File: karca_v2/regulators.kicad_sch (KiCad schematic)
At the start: 23 parts, among them J1 CON_FAN1, J2 Conn_Batt, SW1 SW_SPST, SW2 SW_SPST, SW3 SW_SPST, U1 TVS1400DRV

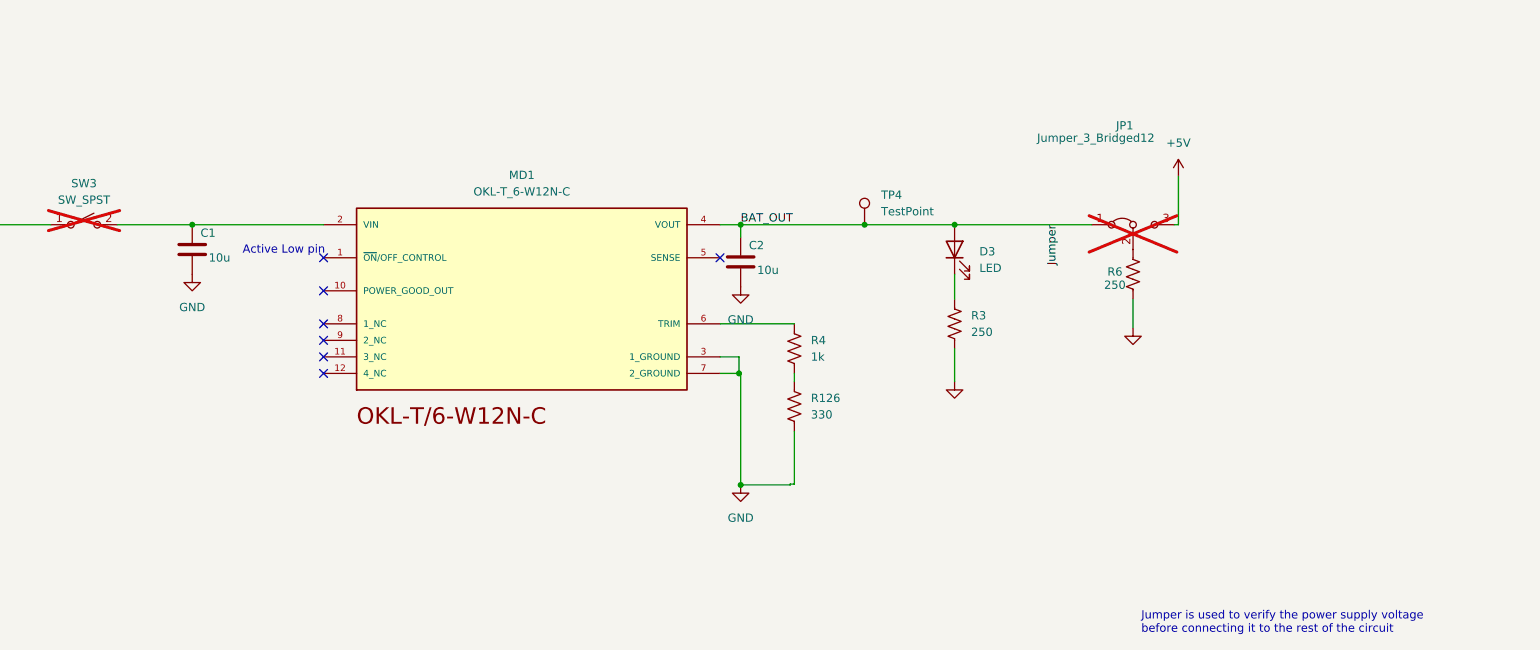
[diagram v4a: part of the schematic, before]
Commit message: finished schematic for v2.1
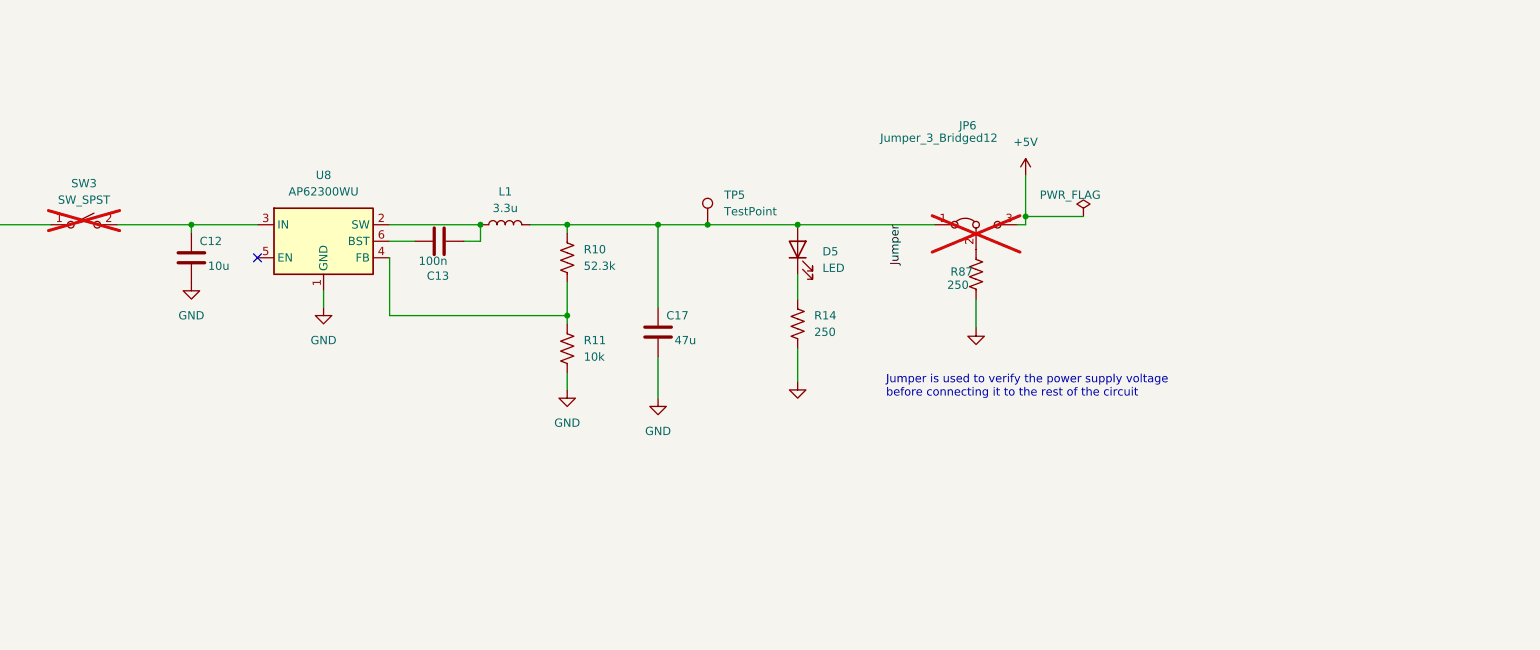
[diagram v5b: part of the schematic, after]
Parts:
- removed C1: 10u, Capacitor_Tantalum_SMD:CP_EIA-3216-18_Kemet-A, symbol Device:C
- removed C2: 10u, Capacitor_SMD:C_1206_3216Metric, symbol Device:C
- removed D3: LED, LED_SMD:LED_1206_3216Metric, symbol Device:LED
- removed JP1: Jumper_3_Bridged12, Connector_PinSocket_2.54mm:PinSocket_1x03_P2.54mm_Vertical, symbol Jumper:Jumper_3_Bridged12
- removed MD1: OKL-T_6-W12N-C, custom-footprints:MURATA_OKL-T-6-W12N-C_0, symbol karca_lib:OKL-T_6-W12N-C
- removed R126: 330, Resistor_SMD:R_1206_3216Metric, symbol Device:R_US
- removed R3, R6: 250, Resistor_SMD:R_1206_3216Metric, symbol Device:R_US
- removed R4: 1k, Resistor_SMD:R_1206_3216Metric, symbol Device:R_US
- removed TP4: TestPoint, TestPoint:TestPoint_Pad_D2.0mm, symbol Connector:TestPoint
- added C12: 10u, Capacitor_SMD:C_0805_2012Metric, symbol Device:C
- added C13: 100n, Capacitor_SMD:C_0805_2012Metric, symbol Device:C
- added C17: 47u, Capacitor_SMD:C_0805_2012Metric, symbol Device:C
- added D5: LED, LED_SMD:LED_1206_3216Metric, symbol Device:LED
- added JP6: Jumper_3_Bridged12, Connector_PinSocket_2.54mm:PinSocket_1x03_P2.54mm_Vertical, symbol Jumper:Jumper_3_Bridged12
- added L1: 3.3u, Inductor_SMD:L_Sunlord_SWPA4020S, symbol Device:L
- added R10: 52.3k, Resistor_SMD:R_1206_3216Metric, symbol Device:R_US
- added R11: 10k, Resistor_SMD:R_1206_3216Metric, symbol Device:R_US
- added R14, R87: 250, Resistor_SMD:R_1206_3216Metric, symbol Device:R_US
- added TP5: TestPoint, TestPoint:TestPoint_Pad_D2.0mm, symbol Connector:TestPoint
- added U8: AP62300WU, Package_TO_SOT_SMD:TSOT-23-6, symbol Regulator_Switching:AP62300WU
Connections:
- net +5V: now also JP6.3 (B)
- net GND: now also C12.2, C17.2, R11.2, R14.2, R87.2, U8.1 (GND)
- net at SW3.2 (B): now also C12.1, U8.3 (IN)
- new net: C13.2, L1.1, U8.2 (SW)
- new net: R10.2, R11.1, U8.4 (FB)
- new net: C13.1, U8.6 (BST)
- new net: JP6.2 (C), R87.1
- new net: D5.1 (K), R14.1
- new net Jumper: C17.1, D5.2 (A), JP6.1 (A), L1.2, R10.1, TP5.1
- no-connect marks 7 -> 1
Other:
- note removed: "Active Low pin"

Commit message: swapped adcs
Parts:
- removed C12: 10u, Capacitor_SMD:C_0805_2012Metric, symbol Device:C
- removed C13: 100n, Capacitor_SMD:C_0805_2012Metric, symbol Device:C
- removed C17: 47u, Capacitor_SMD:C_0805_2012Metric, symbol Device:C
- removed D5: LED, LED_SMD:LED_1206_3216Metric, symbol Device:LED
- removed JP6: Jumper_3_Bridged12, Connector_PinSocket_2.54mm:PinSocket_1x03_P2.54mm_Vertical, symbol Jumper:Jumper_3_Bridged12
- removed L1: 3.3u, Inductor_SMD:L_Sunlord_SWPA4020S, symbol Device:L
- removed R10: 52.3k, Resistor_SMD:R_1206_3216Metric, symbol Device:R_US
- removed R11: 10k, Resistor_SMD:R_1206_3216Metric, symbol Device:R_US
- removed R14, R87: 250, Resistor_SMD:R_1206_3216Metric, symbol Device:R_US
- removed TP5: TestPoint, TestPoint:TestPoint_Pad_D2.0mm, symbol Connector:TestPoint
- removed U8: AP62300WU, Package_TO_SOT_SMD:TSOT-23-6, symbol Regulator_Switching:AP62300WU
- added C1: 10u, Capacitor_Tantalum_SMD:CP_EIA-3216-18_Kemet-A, symbol Device:C
- added C2: 10u, Capacitor_SMD:C_1206_3216Metric, symbol Device:C
- added D3: LED, LED_SMD:LED_1206_3216Metric, symbol Device:LED
- added JP1: Jumper_3_Bridged12, Connector_PinSocket_2.54mm:PinSocket_1x03_P2.54mm_Vertical, symbol Jumper:Jumper_3_Bridged12
- added MD1: OKL-T_6-W12N-C, custom-footprints:MURATA_OKL-T-6-W12N-C_0, symbol karca_lib:OKL-T_6-W12N-C
- added R126: 330, Resistor_SMD:R_1206_3216Metric, symbol Device:R_US
- added R3, R6: 250, Resistor_SMD:R_1206_3216Metric, symbol Device:R_US
- added R4: 1k, Resistor_SMD:R_1206_3216Metric, symbol Device:R_US
- added TP4: TestPoint, TestPoint:TestPoint_Pad_D2.0mm, symbol Connector:TestPoint
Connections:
- net +5V: now also JP1.3 (B)
- net GND: now also C1.2, C2.2, MD1.3 (1_GROUND), MD1.7 (2_GROUND), R126.2, R3.2, R6.2
- net at SW3.2 (B): now also C1.1, MD1.2 (VIN)
- new net: JP1.2 (C), R6.1
- new net: R126.1, R4.2
- new net: MD1.6 (TRIM), R4.1
- new net: D3.1 (K), R3.1
- new net BAT_OUT: C2.1, D3.2 (A), JP1.1 (A), MD1.4 (VOUT), TP4.1
- no-connect marks 1 -> 7
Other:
- note added: "Active Low pin"

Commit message: All tests passed. Going to run DFM next
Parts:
- removed D3: LED, LED_SMD:LED_1206_3216Metric, symbol Device:LED
- removed JP1: Jumper_3_Bridged12, Connector_PinSocket_2.54mm:PinSocket_1x03_P2.54mm_Vertical, symbol Jumper:Jumper_3_Bridged12
- removed MD1: OKL-T_6-W12N-C, custom-footprints:MURATA_OKL-T-6-W12N-C_0, symbol karca_lib:OKL-T_6-W12N-C
- removed R126: 330, Resistor_SMD:R_1206_3216Metric, symbol Device:R_US
- removed R4: 1k, Resistor_SMD:R_1206_3216Metric, symbol Device:R_US
- removed R6: 250, Resistor_SMD:R_1206_3216Metric, symbol Device:R_US
- removed TP4: TestPoint, TestPoint:TestPoint_Pad_D2.0mm, symbol Connector:TestPoint
- added C17: 47u, Capacitor_SMD:C_0805_2012Metric, symbol Device:C
- added D5: LED, LED_SMD:LED_1206_3216Metric, symbol Device:LED
- added JP1: SolderJumper_2_Open, Jumper:SolderJumper-2_P1.3mm_Open_TrianglePad1.0x1.5mm, symbol Jumper:SolderJumper_2_Open
- added L1: 3.3u, Inductor_SMD:L_Sunlord_SWPA4020S, symbol Device:L
- added R11: 10k, Resistor_SMD:R_0603_1608Metric, symbol Device:R_US
- added R14: 250, Resistor_SMD:R_1206_3216Metric, symbol Device:R_US
- added TP5: TestPoint, TestPoint:TestPoint_Pad_D2.0mm, symbol Connector:TestPoint
- added U8: AP62300WU, Package_TO_SOT_SMD:TSOT-23-6, symbol Regulator_Switching:AP62300WU
- C1: value 10u -> 100n; footprint Capacitor_Tantalum_SMD:CP_EIA-3216-18_Kemet-A -> Capacitor_SMD:C_0805_2012Metric
- C2: footprint Capacitor_SMD:C_1206_3216Metric -> Capacitor_SMD:C_0805_2012Metric
- R3: value 250 -> 52.3k; footprint Resistor_SMD:R_1206_3216Metric -> Resistor_SMD:R_0603_1608Metric
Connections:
- net BAT_OUT is gone; now on net 12v_in: C2.1
- net +5V: now also JP1.2 (B)
- net GND: now also C17.2, R11.2, R14.2, U8.1 (GND); no longer C1.2, R3.2
- net 12v_in: now reaches SW3.2 (B)
- net 12v_in: now also U8.3 (IN); no longer C1.1
- net Jumper: now reaches R3.1
- net Jumper: now also C17.1, D5.2 (A), JP1.1 (A), L1.2, TP5.1
- new net: D5.1 (K), R14.1
- new net bst: C1.1, U8.6 (BST)
- new net sw: C1.2, L1.1, U8.2 (SW)
- new net v_fb: R11.1, R3.2, U8.4 (FB)
- no-connect marks 7 -> 1
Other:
- note removed: "Active Low pin"

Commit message: changed diode to SMD schottky and fixed switches
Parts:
- removed J1: CON_FAN1, custom-footprints:P-2604-1102, symbol Connector:Screw_Terminal_01x02
- removed SW1, SW2, SW3: SW_SPST, custom-footprints:SW_500SSP1S2M2QEA, symbol Switch:SW_SPST
- added SW2, SW4: SW_SPDT_MSM, custom-footprints:SW_500SSP1S2M2QEA, symbol Switch:SW_SPDT_MSM
- D1: value 90SQ035 -> SDT10A45P5; footprint Diode_THT:D_DO-201AD_P15.24mm_Horizontal -> Diode_SMD:D_PowerDI-5; now fitted; now in the parts list
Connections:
- net +12V: now also SW2.3 (4)
- net 12v_in: now also SW2.2 (3)
- net diode_in: now reaches D1.2 (A)
- net diode_in: now also SW4.3 (4)
- net at F1.2: now also SW4.2 (3)
- no-connect marks 1 -> 3
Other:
- note removed: "polarity protection"
- moved on the sheet: C1, C17, C2, D2, D5, F1, J2, JP1, L1, R1, R11, R14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
